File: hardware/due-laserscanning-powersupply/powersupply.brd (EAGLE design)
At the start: 100 x 80 mm, 14 parts, among them IC1 7805TV, X1 MKDSN1,5/3-5,08, X2 MKDSN1,5/2-5,08, X3 1751251, X4 BU-SMA-V, X5 BU-SMA-V, X6 BU-SMA-V, X7 MKDSN1,5/2-5,08

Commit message: update powersupply board
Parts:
- added C1, C2, C3, C4, C5, C6: (no value), rcl:C0805
- added X8: MKDSN1,5/2-5,08, con-phoenix-508:MKDSN1,5/2-5,08
- moved X2 6.35 mm to (80.0, 5.08)
- moved X1 5.72 mm to (34.9, 5.08)
- moved X3 5.08 mm to (59.7, 74.9)
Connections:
- net GND: now also C1.2, C2.2, C3.2, C4.2, C5.2, C6.2, X4.2, X4.3, X4.4, X4.5, X5.2, X5.3, X5.4, X5.5, X6.2, X6.3, X6.4, X6.5, X8.1
- net N$10: now also C3.1
- net N$6: now also X8.2
- net N$7: now also C4.1, C5.1, C6.1
- net N$8: now also C1.1
- net N$9: now also C2.1
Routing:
- net N$6: track 48.2 -> 138.8 mm
- net N$1: track 65.8 -> 68.4 mm
- net N$2: track 64.3 -> 66.9 mm
- net N$5: track 38.0 -> 40.3 mm
- net N$3: track 11.2 -> 13.6 mm
- net N$4: track 24.9 -> 27.3 mm

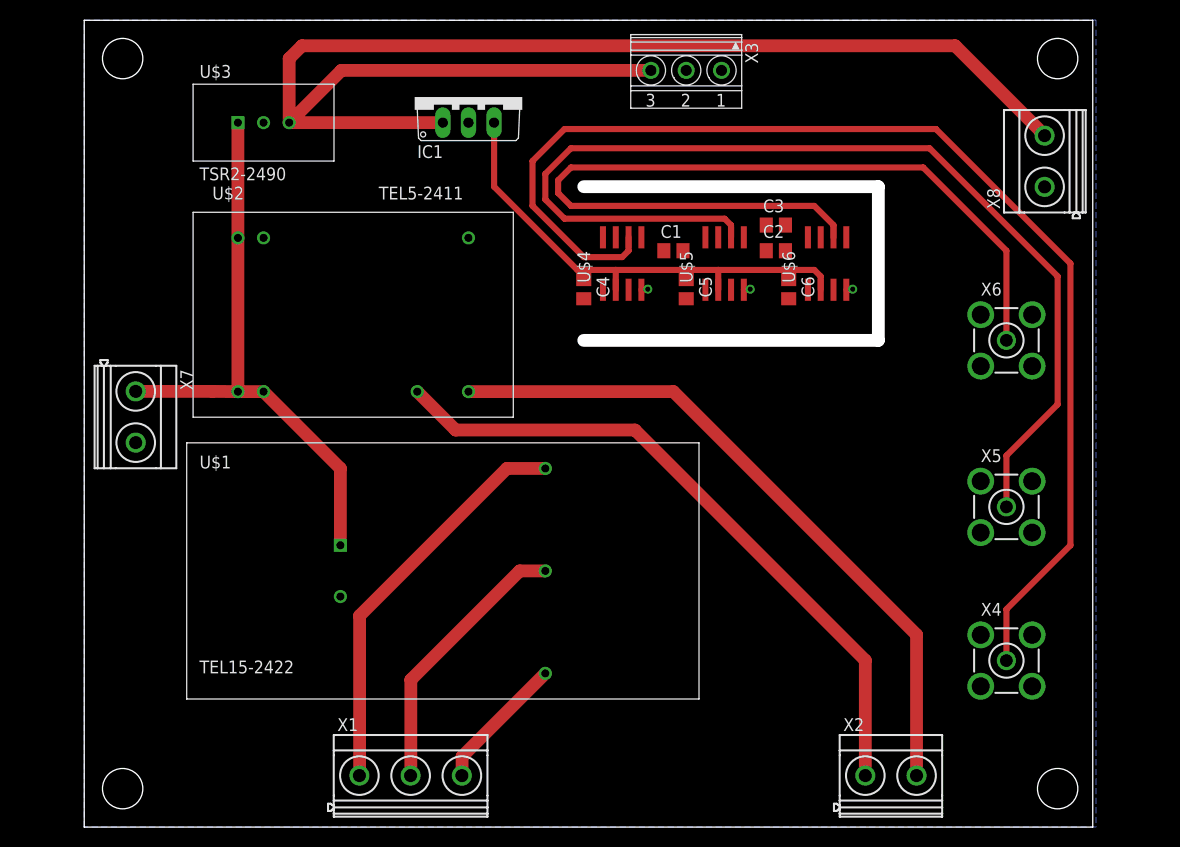
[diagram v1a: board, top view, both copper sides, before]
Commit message: first revision of powersupply board was a total failure due to small holes and mirrored components
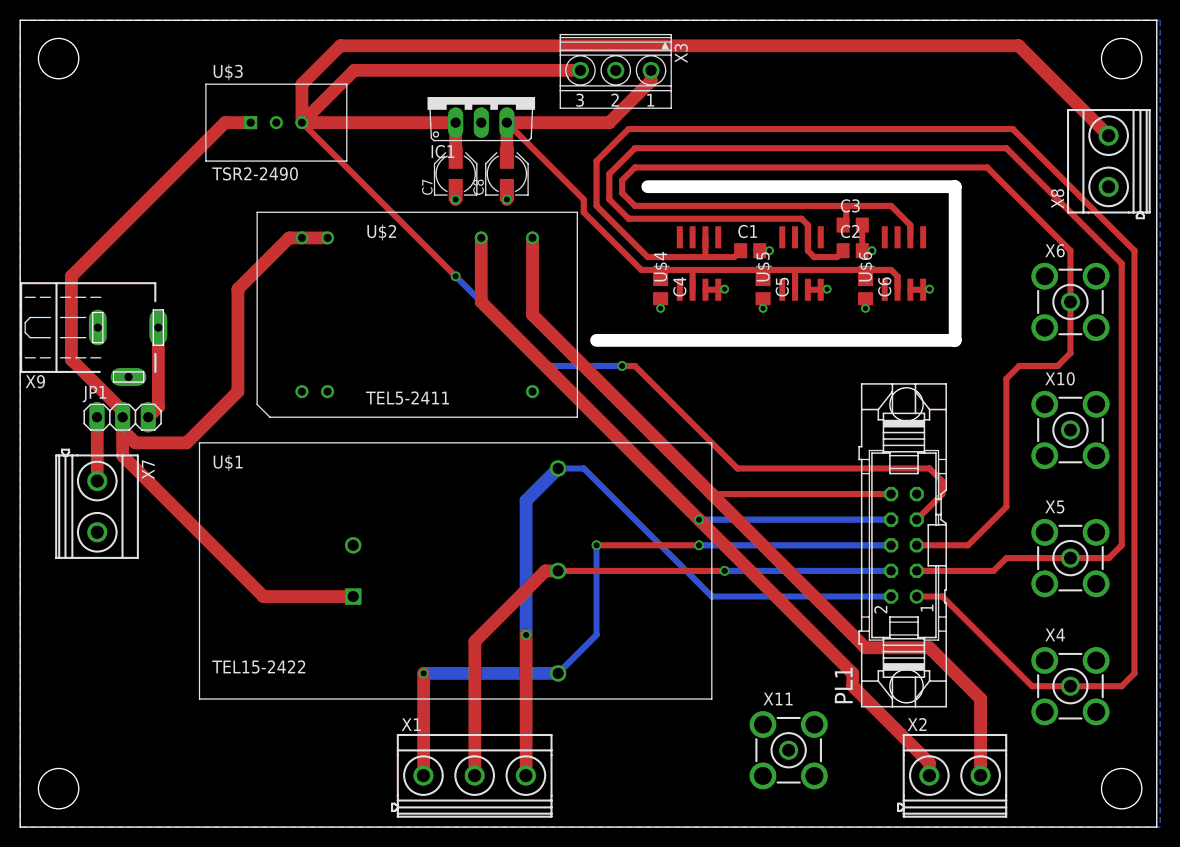
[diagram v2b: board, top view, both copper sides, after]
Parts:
- added C7, C8: 10u, rcl:PANASONIC_B
- added JP1: (no value), pinhead:1X03
- added PL1: (no value), con-harting-v:10V
- added X10, X11: BU-SMA-V, con-coax:BU-SMA-V
- added X9: NEB21R, con-lumberg:NEB21R
- moved X7 9.67 mm to (1.27, 31.8)
- moved X5 8.13 mm to (97.8, 26.7)
- moved C1 7.62 mm to (66.0, 57.1)
- moved C2 7.62 mm to (76.2, 57.1)
- moved C3 7.62 mm to (76.2, 59.7)
- moved C5 7.62 mm to (67.3, 53.3)
- moved C6 7.62 mm to (77.5, 53.3)
- moved U$5 7.62 mm to (71.1, 55.9)
- moved U$6 7.62 mm to (81.3, 55.9)
- moved C4 7.62 mm to (57.1, 53.3)
- moved U$4 7.62 mm to (61.0, 55.9)
- moved X6 7.41 mm to (97.8, 52.1)
- moved X3 6.98 mm to (52.7, 74.9)
- moved X4 6.84 mm to (97.8, 14.0)
- moved U$2 6.35 mm to (16.5, 40.6)
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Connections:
- removed net N$1: U$2.14, X2.2
- removed net N$10: C3.1, U$6.6, X6.1
- removed net N$2: U$2.16, X2.1
- removed net N$3: U$1.5, X1.3
- removed net N$4: U$1.4, X1.2
- removed net N$5: U$1.3, X1.1
- removed net N$6: IC1.1, U$3.3, X3.3, X8.2
- removed net N$7: C4.1, C5.1, C6.1, IC1.3, U$4.2, U$5.2, U$6.2
- removed net N$8: C1.1, U$4.6, X4.1
- removed net N$9: C2.1, U$5.6, X5.1
- new net +5V: C4.1, C5.1, C6.1, C8.+, IC1.3, U$4.2, U$5.2, U$6.2, X3.1
- new net -12V: PL1.2, U$1.5, X1.3
- new net 12V: PL1.6, U$1.3, X1.1
- new net 12VCOM: PL1.4, U$1.4, X1.2
- new net 2V5: C3.1, PL1.5, U$6.6, X6.1
- new net 3V: C2.1, PL1.3, U$5.6, X5.1
- new net 3V3: C1.1, PL1.1, U$4.6, X4.1
- new net 5VCOM: PL1.8, U$2.16, X2.1
- new net 5VISO: PL1.10, U$2.14, X2.2
- new net 9V: C7.+, IC1.1, PL1.7, U$3.3, X3.3, X8.2
- new net N$11: JP1.1, X7.1
- new net N$12: JP1.3, X9.1
- net GND: now also C7.-, C8.-, PL1.9, U$4.3, U$5.3, U$6.3, X10.1, X10.2, X10.3, X10.4, X10.5, X11.1, X11.2, X11.3, X11.4, X11.5, X9.3
- net VCC: now also JP1.2; no longer X7.1
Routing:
- net 9V: track 0.00 -> 220.6 mm, vias 0 -> 2
- net 3V3: track 0.00 -> 150.4 mm
- net N$6: track 138.8 -> 0.00 mm
- net 3V: track 0.00 -> 135.7 mm
- net 2V5: track 0.00 -> 123.5 mm
- net N$8: track 119.8 -> 0.00 mm
- net N$9: track 105.3 -> 0.00 mm
- net 5VISO: track 0.00 -> 93.2 mm
- net 5VCOM: track 0.00 -> 90.8 mm, vias 0 -> 1
- net N$10: track 88.4 -> 0.00 mm
- net +5V: track 0.00 -> 75.7 mm
- net -12V: track 0.00 -> 70.1 mm, vias 0 -> 1
- net N$1: track 68.4 -> 0.00 mm
- net 12V: track 0.00 -> 67.0 mm, vias 0 -> 3
- net N$2: track 66.9 -> 0.00 mm
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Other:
- board size 100 x 80 mm -> 112.7 x 80 mm
